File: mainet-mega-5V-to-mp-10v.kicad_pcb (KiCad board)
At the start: 2 copper layers, 43.2 x 67.3 mm, 12 parts, among them J1 Screw_Terminal_01x03, J2 Screw_Terminal_01x03, Q1 2N3906, Q2 BUK9518-55, U1 4N38

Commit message: PCB V0.1
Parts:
- moved Q1 8.03 mm to (133.3, 130.8), turned to 90 degrees
- moved J1 0.16 mm to (114.5, 139.7)
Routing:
- net Net-(Q1-Pad1): track 8.20 -> 17.5 mm
- net /GNDD: track 13.4 -> 16.9 mm
- net Net-(Q2-Pad1): track 37.5 -> 39.4 mm
- net Net-(D1-Pad2): track 9.33 -> 10.5 mm

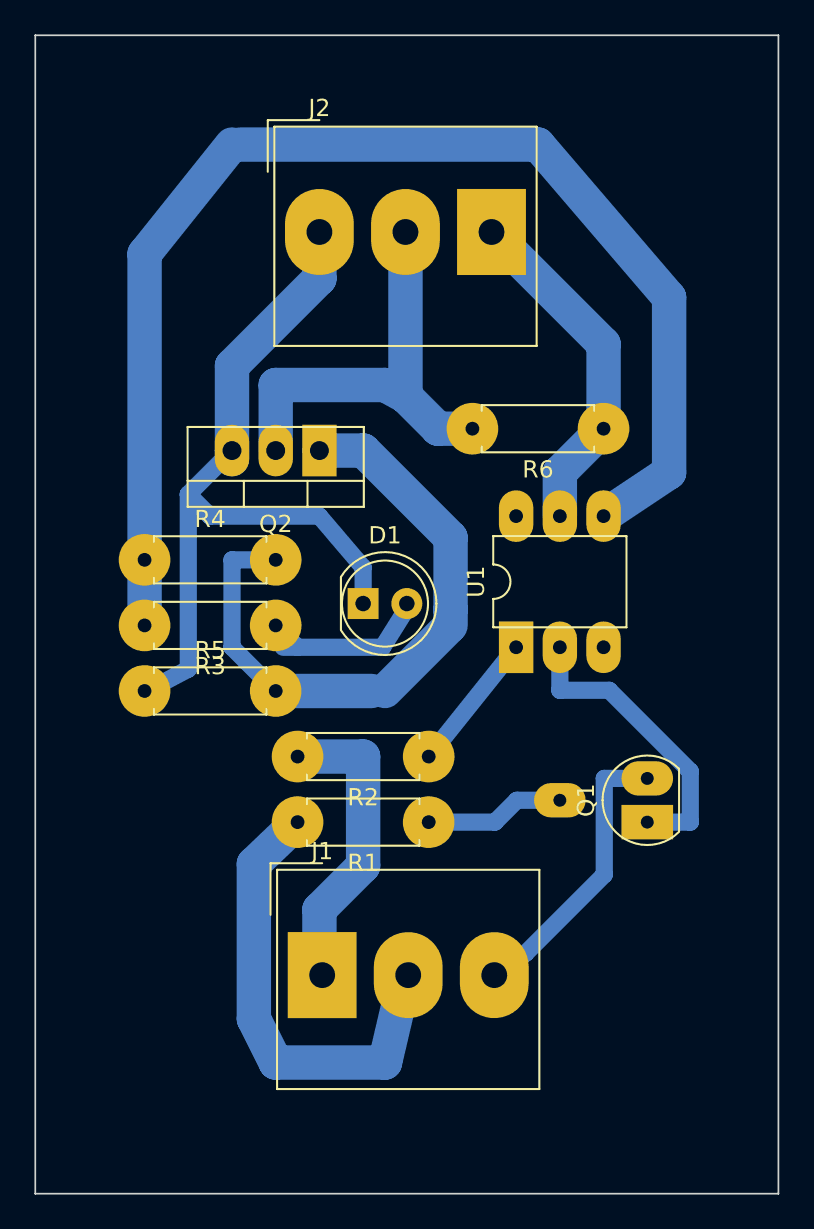
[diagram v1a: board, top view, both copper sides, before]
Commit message: Correción de pistas
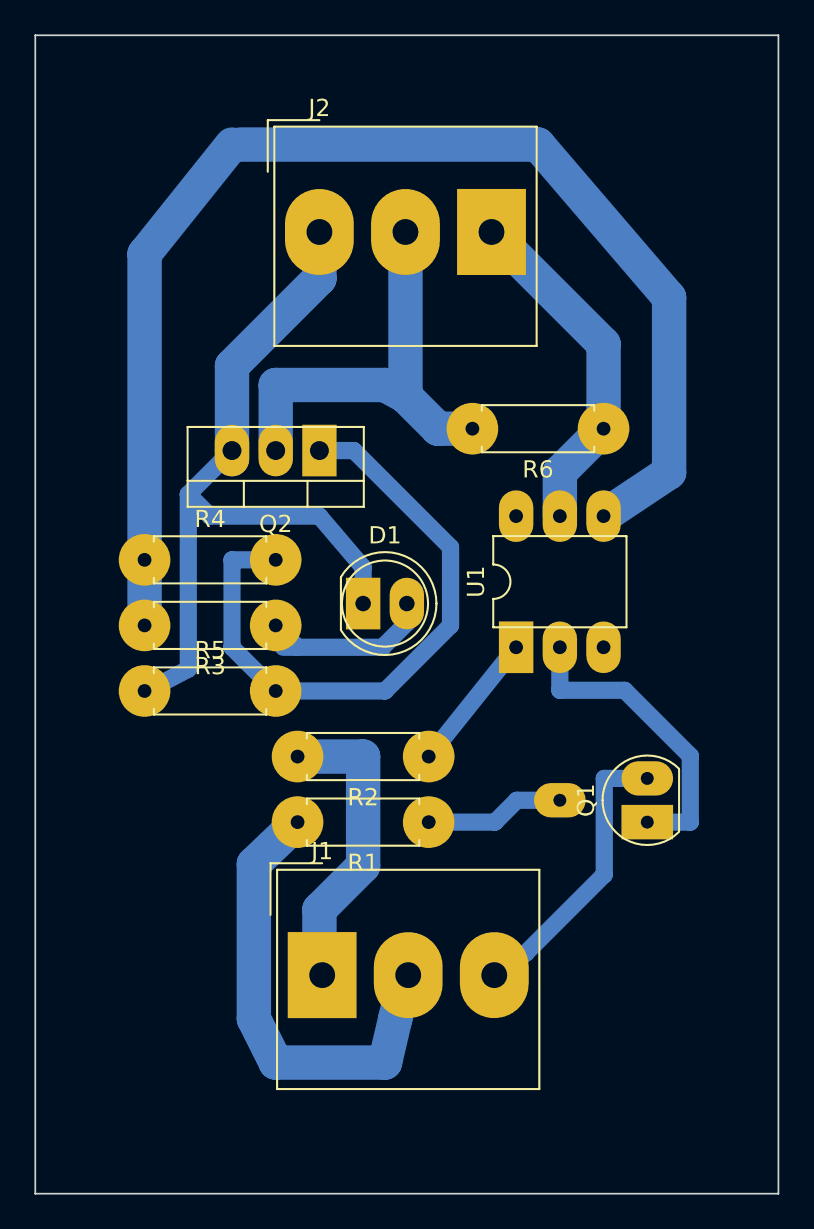
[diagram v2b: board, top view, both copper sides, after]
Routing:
- net Net-(J1-Pad2): track 26.9 -> 29.8 mm
- net /+5V: track 17.6 -> 19.5 mm
- net Net-(Q2-Pad1): track 39.4 -> 38.2 mm
- net /GNDD: track 16.9 -> 18.0 mm
- net Net-(Q1-Pad1): track 17.5 -> 18.0 mm

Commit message: KICAD: Modificar PCB: 5v-to-mp-10v
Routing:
- net Net-(J1-Pad2): track 29.8 -> 27.2 mm
- net Net-(Q1-Pad1): track 18.0 -> 20.6 mm
- net Net-(J2-Pad2): track 25.7 -> 27.7 mm
- net /+5V: track 19.5 -> 18.5 mm
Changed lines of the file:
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@@
     (thickness 1.6)
     (drawings 4)
-    (tracks 76)
+    (tracks 73)
     (zones 0)
     (modules 12)
@@
   (segment (start 107.95 113.03) (end 106.68 111.76) (width 1) (layer B.Cu) (net 1))
   (segment (start 104.275 123.19) (end 104.14 123.19) (width 1.5998) (layer B.Cu) (net 1))
-  (segment (start 114.3 96.52) (end 114.3 99.2203) (width 2) (layer B.Cu) (net 1))
-  (segment (start 114.3 99.2203) (end 109.22 104.3) (width 2) (layer B.Cu) (net 1))
-  (segment (start 109.22 104.3) (end 109.22 109.22) (width 2) (layer B.Cu) (net 1))
+  (segment (start 114.3 96.52) (end 114.3 99.2203) (width 1) (layer B.Cu) (net 1))
+  (segment (start 114.3 99.2203) (end 109.22 104.3) (width 1) (layer B.Cu) (net 1))
+  (segment (start 109.22 104.3) (end 109.22 109.22) (width 1) (layer B.Cu) (net 1))
   (segment (start 109.22 109.722) (end 109.22 109.22) (width 2) (layer B.Cu) (net 1))
   (segment (start 109.22 109.22) (end 106.68 111.76) (width 1) (layer B.Cu) (net 1))
@@
   (segment (start 118.705 142.24) (end 119.46 141.485) (width 1) (layer B.Cu) (net 4))
   (segment (start 119.46 141.485) (end 119.46 139.7) (width 1) (layer B.Cu) (net 4))
-  (segment (start 118.705 142.24) (end 119.3 139.7) (width 2) (layer B.Cu) (net 4))
-  (segment (start 113.03 130.81) (end 110.49 133.241) (width 2) (layer B.Cu) (net 4))
-  (segment (start 110.49 133.241) (end 110.49 142.24) (width 2) (layer B.Cu) (net 4))
-  (segment (start 110.49 142.24) (end 111.76 144.78) (width 2) (layer B.Cu) (net 4))
-  (segment (start 111.76 144.78) (end 118.11 144.78) (width 2) (layer B.Cu) (net 4))
-  (segment (start 118.11 144.78) (end 118.705 142.24) (width 2) (layer B.Cu) (net 4))
+  (segment (start 113.03 130.81) (end 110.49 133.241) (width 1) (layer B.Cu) (net 4))
+  (segment (start 110.49 133.241) (end 110.49 142.24) (width 1) (layer B.Cu) (net 4))
+  (segment (start 110.49 142.24) (end 111.76 144.78) (width 1) (layer B.Cu) (net 4))
+  (segment (start 111.76 144.78) (end 118.11 144.78) (width 1) (layer B.Cu) (net 4))
+  (segment (start 118.11 144.78) (end 118.705 142.24) (width 1) (layer B.Cu) (net 4))
   (segment (start 114.3 137.795) (end 114.46 137.955) (width 1) (layer B.Cu) (net 5))
   (segment (start 114.46 137.955) (end 114.46 139.7) (width 1) (layer B.Cu) (net 5))
   (segment (start 114.3 137.795) (end 114.3 139.7) (width 2) (layer B.Cu) (net 5))
-  (segment (start 113.03 127) (end 116.84 127) (width 2) (layer B.Cu) (net 5))
-  (segment (start 116.84 127) (end 116.84 133.35) (width 2) (layer B.Cu) (net 5))
-  (segment (start 116.84 133.35) (end 114.3 135.89) (width 2) (layer B.Cu) (net 5))
-  (segment (start 114.3 135.89) (end 114.3 137.795) (width 2) (layer B.Cu) (net 5))
-  (segment (start 119.3 106.06) (end 119.3 96.52) (width 2) (layer B.Cu) (net 6))
-  (segment (start 123.19 107.95) (end 121.19 107.95) (width 2) (layer B.Cu) (net 6))
-  (segment (start 121.19 107.95) (end 119.3 106.06) (width 2) (layer B.Cu) (net 6))
-  (segment (start 119.3 106.06) (end 118.11 105.41) (width 2) (layer B.Cu) (net 6))
-  (segment (start 118.11 105.41) (end 111.76 105.41) (width 2) (layer B.Cu) (net 6))
-  (segment (start 111.76 105.41) (end 111.76 109.22) (width 2) (layer B.Cu) (net 6))
-  (segment (start 130.81 107.95) (end 130.81 103.03) (width 2) (layer B.Cu) (net 7))
-  (segment (start 130.81 103.03) (end 124.3 96.52) (width 2) (layer B.Cu) (net 7))
-  (segment (start 128.27 113.03) (end 128.27 110.49) (width 2) (layer B.Cu) (net 7))
-  (segment (start 128.27 110.49) (end 130.81 107.95) (width 2) (layer B.Cu) (net 7))
+  (segment (start 114.3 135.89) (end 114.3 137.795) (width 1) (layer B.Cu) (net 5))
+  (segment (start 116.84 133.35) (end 114.3 135.89) (width 1) (layer B.Cu) (net 5))
+  (segment (start 113.03 127) (end 116.84 128.27) (width 1) (layer B.Cu) (net 5))
+  (segment (start 116.84 128.27) (end 116.84 133.35) (width 1) (layer B.Cu) (net 5))
+  (segment (start 123.19 107.95) (end 119.38 102.87) (width 1) (layer B.Cu) (net 6))
+  (segment (start 118.11 97.71) (end 119.3 96.52) (width 1) (layer B.Cu) (net 6))
+  (segment (start 119.38 102.87) (end 119.3 96.52) (width 1) (layer B.Cu) (net 6))
+  (segment (start 111.76 106.68) (end 111.76 109.22) (width 1) (layer B.Cu) (net 6))
+  (segment (start 119.38 99.06) (end 111.76 106.68) (width 1) (layer B.Cu) (net 6))
+  (segment (start 130.81 107.95) (end 130.81 103.03) (width 1) (layer B.Cu) (net 7))
+  (segment (start 130.81 103.03) (end 124.3 96.52) (width 1) (layer B.Cu) (net 7))
+  (segment (start 128.27 113.03) (end 128.27 110.49) (width 1) (layer B.Cu) (net 7))
+  (segment (start 128.27 110.49) (end 130.81 107.95) (width 1) (layer B.Cu) (net 7))
   (segment (start 120.65 130.81) (end 124.5 130.81) (width 1) (layer B.Cu) (net 8))
   (segment (start 124.5 130.81) (end 125.77 129.54) (width 1) (layer B.Cu) (net 8))
   (segment (start 125.77 129.54) (end 128.27 129.54) (width 1) (layer B.Cu) (net 8))
-  (segment (start 135.85 130.81) (end 133.35 130.81) (width 1) (layer B.Cu) (net 9))
-  (segment (start 135.85 126.96) (end 135.85 130.81) (width 1) (layer B.Cu) (net 9))
-  (segment (start 132.04 123.15) (end 135.85 126.96) (width 1) (layer B.Cu) (net 9))
-  (segment (start 128.27 120.65) (end 128.27 123.15) (width 1) (layer B.Cu) (net 9))
-  (segment (start 128.27 123.15) (end 132.04 123.15) (width 1) (layer B.Cu) (net 9))
+  (segment (start 128.27 124.46) (end 137.16 125.73) (width 1) (layer B.Cu) (net 9))
+  (segment (start 128.27 120.65) (end 128.27 124.46) (width 1) (layer B.Cu) (net 9))
+  (segment (start 137.16 125.73) (end 137.16 129.54) (width 1) (layer B.Cu) (net 9))
+  (segment (start 137.16 129.54) (end 133.35 130.81) (width 1) (layer B.Cu) (net 9))
   (segment (start 111.76 123.19) (end 111.76 122.44) (width 1) (layer B.Cu) (net 10))
   (segment (start 111.76 123.19) (end 109.22 120.65) (width 1) (layer B.Cu) (net 10))
@@
   (segment (start 118.11 123.19) (end 121.92 119.38) (width 1) (layer B.Cu) (net 10))
   (segment (start 125.73 120.65) (end 120.65 127) (width 1) (layer B.Cu) (net 11))
-  (segment (start 104.14 115.57) (end 104.14 119.38) (width 2) (layer B.Cu) (net 12))
-  (segment (start 109.22 91.44) (end 104.14 97.79) (width 2) (layer B.Cu) (net 12))
-  (segment (start 104.14 97.79) (end 104.14 115.57) (width 2) (layer B.Cu) (net 12))
-  (segment (start 130.81 113.03) (end 134.62 110.49) (width 2) (layer B.Cu) (net 12))
-  (segment (start 134.62 110.49) (end 134.62 100.33) (width 2) (layer B.Cu) (net 12))
-  (segment (start 134.62 100.33) (end 127 91.44) (width 2) (layer B.Cu) (net 12))
-  (segment (start 127 91.44) (end 109.707 91.44) (width 2) (layer B.Cu) (net 12))
+  (segment (start 104.14 115.57) (end 104.14 119.38) (width 1) (layer B.Cu) (net 12))
+  (segment (start 109.22 91.44) (end 104.14 97.79) (width 1) (layer B.Cu) (net 12))
+  (segment (start 104.14 97.79) (end 104.14 115.57) (width 1) (layer B.Cu) (net 12))
+  (segment (start 130.81 113.03) (end 134.62 110.49) (width 1) (layer B.Cu) (net 12))
+  (segment (start 134.62 110.49) (end 134.62 100.33) (width 1) (layer B.Cu) (net 12))
+  (segment (start 134.62 100.33) (end 127 91.44) (width 1) (layer B.Cu) (net 12))
+  (segment (start 127 91.44) (end 109.707 91.44) (width 1) (layer B.Cu) (net 12))
   (segment (start 109.707 91.44) (end 109.22 91.44) (width 1) (layer B.Cu) (net 12))
 )

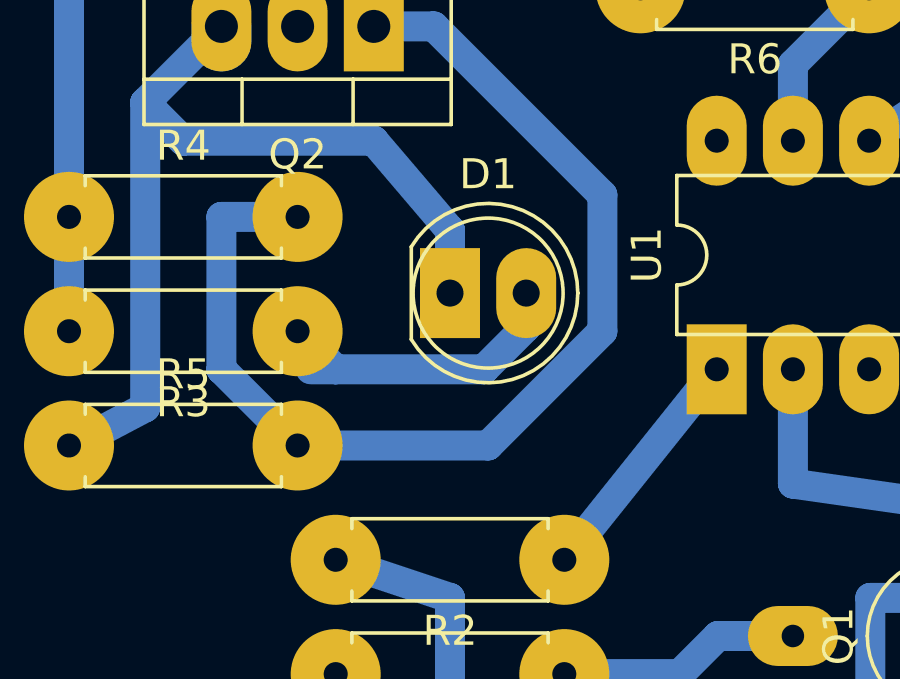
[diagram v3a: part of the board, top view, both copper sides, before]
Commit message: KICAD: Modificar PCB mainet-mega-5v-to-mp-10v
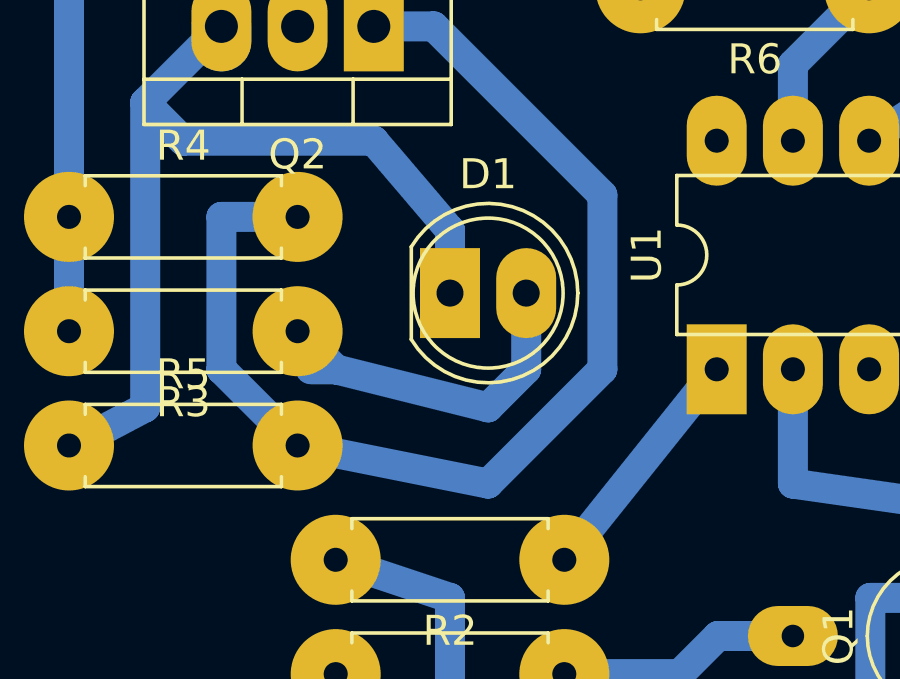
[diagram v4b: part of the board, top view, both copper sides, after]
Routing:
- net Net-(D1-Pad2): track 10.7 -> 12.2 mm
- net Net-(Q2-Pad1): track 38.2 -> 39.6 mm
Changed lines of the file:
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@@
     (thickness 1.6)
     (drawings 4)
-    (tracks 73)
+    (tracks 72)
     (zones 0)
     (modules 12)
@@
   (segment (start 109.22 109.722) (end 109.22 109.22) (width 2) (layer B.Cu) (net 1))
   (segment (start 109.22 109.22) (end 106.68 111.76) (width 1) (layer B.Cu) (net 1))
-  (segment (start 117.967 120.65) (end 119.38 119.237) (width 1) (layer B.Cu) (net 2))
-  (segment (start 119.38 119.237) (end 119.38 118.401) (width 1) (layer B.Cu) (net 2))
-  (segment (start 113.03 120.65) (end 117.967 120.65) (width 1) (layer B.Cu) (net 2))
   (segment (start 111.76 119.38) (end 113.03 120.65) (width 1) (layer B.Cu) (net 2))
   (segment (start 112.194 120.65) (end 113.03 120.65) (width 1) (layer B.Cu) (net 2))
-  (segment (start 119.38 118.401) (end 119.38 118.11) (width 1) (layer B.Cu) (net 2))
+  (segment (start 119.38 120.65) (end 119.38 118.11) (width 1) (layer B.Cu) (net 2))
+  (segment (start 113.03 120.65) (end 118.11 121.92) (width 1) (layer B.Cu) (net 2))
+  (segment (start 118.11 121.92) (end 119.38 120.65) (width 1) (layer B.Cu) (net 2))
   (segment (start 125.2925 139.065) (end 125.095 139.065) (width 1) (layer B.Cu) (net 3))
   (segment (start 125.095 139.065) (end 124.46 139.7) (width 1) (layer B.Cu) (net 3))
@@
   (segment (start 116.3 109.22) (end 114.3 109.22) (width 1) (layer B.Cu) (net 10))
   (segment (start 121.92 114.84) (end 116.3 109.22) (width 1) (layer B.Cu) (net 10))
-  (segment (start 121.92 119.38) (end 121.92 114.84) (width 1) (layer B.Cu) (net 10))
-  (segment (start 111.76 123.19) (end 118.11 123.19) (width 1) (layer B.Cu) (net 10))
-  (segment (start 118.11 123.19) (end 121.92 119.38) (width 1) (layer B.Cu) (net 10))
+  (segment (start 121.92 120.65) (end 121.92 114.84) (width 1) (layer B.Cu) (net 10))
+  (segment (start 111.76 123.19) (end 118.11 124.46) (width 1) (layer B.Cu) (net 10))
+  (segment (start 118.11 124.46) (end 121.92 120.65) (width 1) (layer B.Cu) (net 10))
   (segment (start 125.73 120.65) (end 120.65 127) (width 1) (layer B.Cu) (net 11))
   (segment (start 104.14 115.57) (end 104.14 119.38) (width 1) (layer B.Cu) (net 12))
